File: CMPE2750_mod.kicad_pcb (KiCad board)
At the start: 6 copper layers, 213.4 x 152.4 mm, 337 parts, among them J1 Conn_02x07_Odd_Even, J10 Conn_01x02, J2 Conn_02x04_Odd_Even, J3 Conn_02x16_Odd_Even, J4 Conn_01x16, J5 Conn_01x04, J6 USB4510-03-1-A, J7 Conn_02x02_Odd_Even, J8 Conn_02x02_Odd_Even, J9 Conn_01x02, Q1 IRLML6402TRPBF, Q10 2N7002, Q11 2N7002, Q12 2N7002, Q13 2N7002, Q14 2N7002, Q15 2N7002, Q16 2N7002, Q17 2N7002, Q18 2N7002, Q19 IRLML6402TRPBF, Q2 IRLML6402TRPBF, Q20 IRLML6402TRPBF, Q21 IRLML6402TRPBF, Q22 IRLML6402TRPBF, Q23 IRLML6402TRPBF, Q24 IRLML6402TRPBF, Q25 IRLML6402TRPBF, Q26 IRLML6402TRPBF, Q27 IRLML6402TRPBF, Q28 2N7002, Q29 2N7002, Q3 IRLML6402TRPBF, Q30 2N7002, Q31 2N7002, Q32 2N7002, Q33 2N7002, Q34 2N7002, Q35 2N7002, Q36 2N7002, Q37 2N7002, Q38 2N7002, Q39 2N7002, Q4 IRLML6402TRPBF, Q40 2N7002, Q41 2N7002, Q42 2N7002, Q43 2N7002, Q44 2N7002, Q45 2N7002, Q46 2N7002, Q47 2N7002, Q48 2N7002, Q49 2N7002, Q5 IRLML6402TRPBF, Q50 2N7002, Q51 2N7002, Q52 2N7002, Q53 2N7002, Q54 2N7002, Q55 2N7002, Q56 2N7002, Q57 2N7002, Q58 2N7002, Q59 2N7002, Q6 IRLML6402TRPBF, Q60 2N7002, Q61 2N7002, Q62 2N7002, Q63 2N7002, Q64 2N7002, Q65 2N7002, Q66 2N7002, Q7 IRLML6402TRPBF, Q8 IRLML6402TRPBF, Q9 IRLML6402TRPBF, SW1 D6R90F1LFS, SW2 DS04-254-1L-08BK, SW3 DS04-254-1L-08BK, U1 STM32L476RGTx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

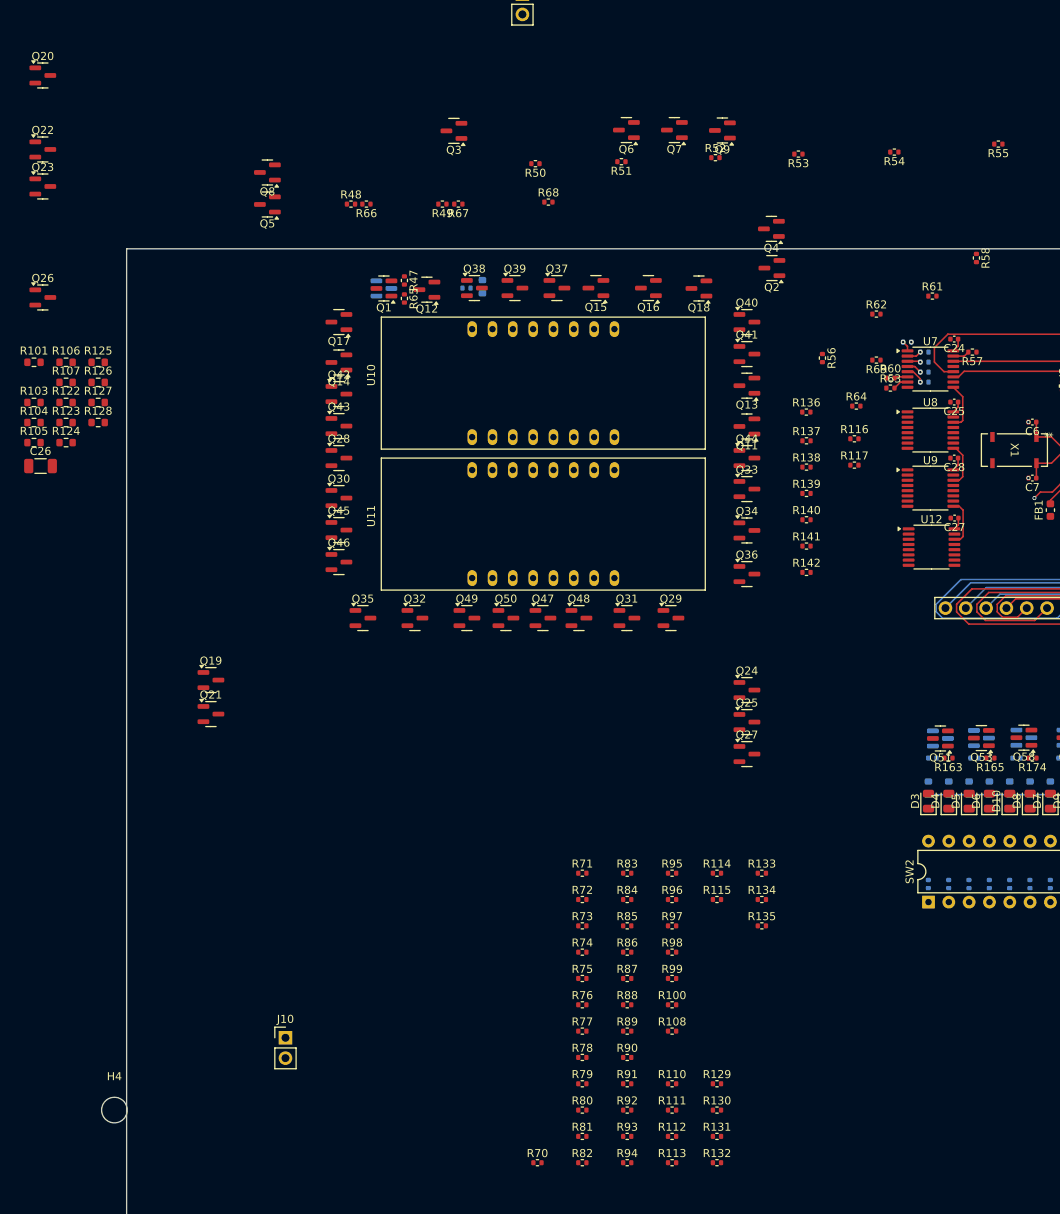
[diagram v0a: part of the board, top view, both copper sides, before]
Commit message: Component placing partly done. Saving before overwriting the pcb with the templating script output
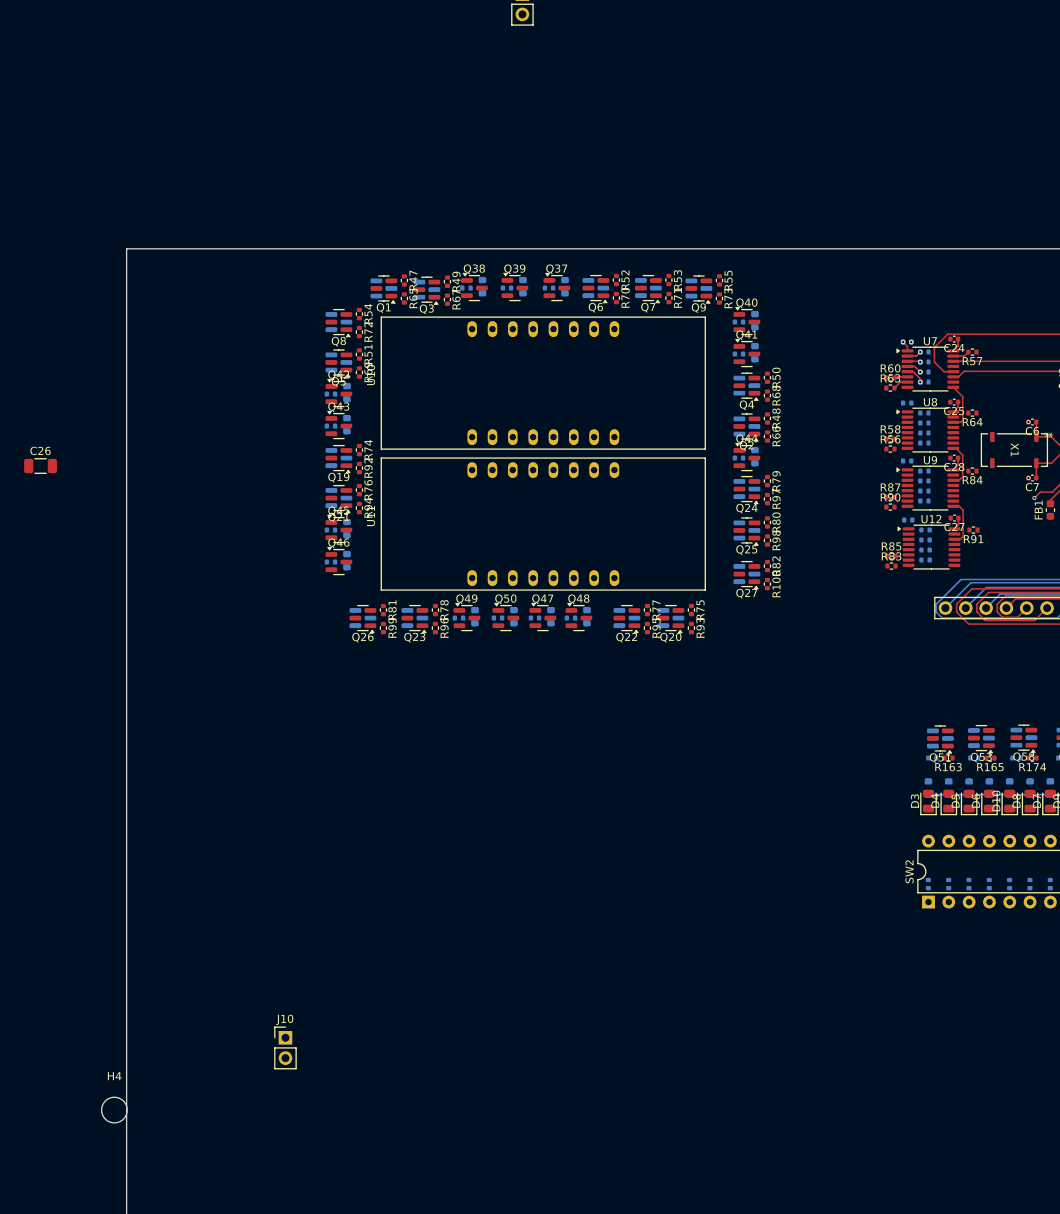
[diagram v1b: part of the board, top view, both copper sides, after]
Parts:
- Q11, Q12, Q13, Q14, Q15, Q16, Q17, Q18, Q28, Q29, Q30, Q31, Q32, Q33, Q34, Q35, Q36, R101, R103, R104, R105, R106, R107, R108, R110, R111, R112, R113, R114, R115, R116, R117, R122, R123, R124, R125, R126, R127, R128, R129, R130, R131, R132, R133, R134, R135, R136, R137, R138, R139, R140, R141, R142, R61, R62, R86, R88, R89: moved to B.Cu
- moved R70 108.5 mm to (92.8, 62.0), turned to -90 degrees
- moved R113 105.1 mm to (57.1, 74.0), turned to 180 degrees
- moved Q20 103.8 mm to (99.6, 102.0), turned to 180 degrees
- moved R110 101.6 mm to (79.1, 60.8), turned to 180 degrees
- moved R111 98.9 mm to (108.1, 65.0), turned to 180 degrees
- moved R112 98.1 mm to (108.1, 69.0), turned to 180 degrees
- moved R108 94.1 mm to (84.3, 60.8), turned to 180 degrees
- moved Q22 93.6 mm to (94.1, 102.0), turned to 180 degrees
- moved R104 91.0 mm to (110.1, 64.8), turned to 90 degrees
- moved R105 90.8 mm to (110.1, 68.8), turned to 90 degrees
- moved R94 88.4 mm to (60.6, 88.2), turned to -90 degrees
- moved R130 87.1 mm to (57.1, 91.0), turned to 180 degrees
- moved R92 87.0 mm to (60.6, 83.2), turned to -90 degrees
- moved R131 86.5 mm to (57.1, 95.0), turned to 180 degrees
- moved R122 86.4 mm to (110.1, 81.8), turned to 90 degrees
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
